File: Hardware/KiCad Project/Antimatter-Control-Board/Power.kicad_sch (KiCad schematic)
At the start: 5 parts, among them J1 3P JST XH, SW1 SW_SPST, U2 AP2210N-3.3TRG1

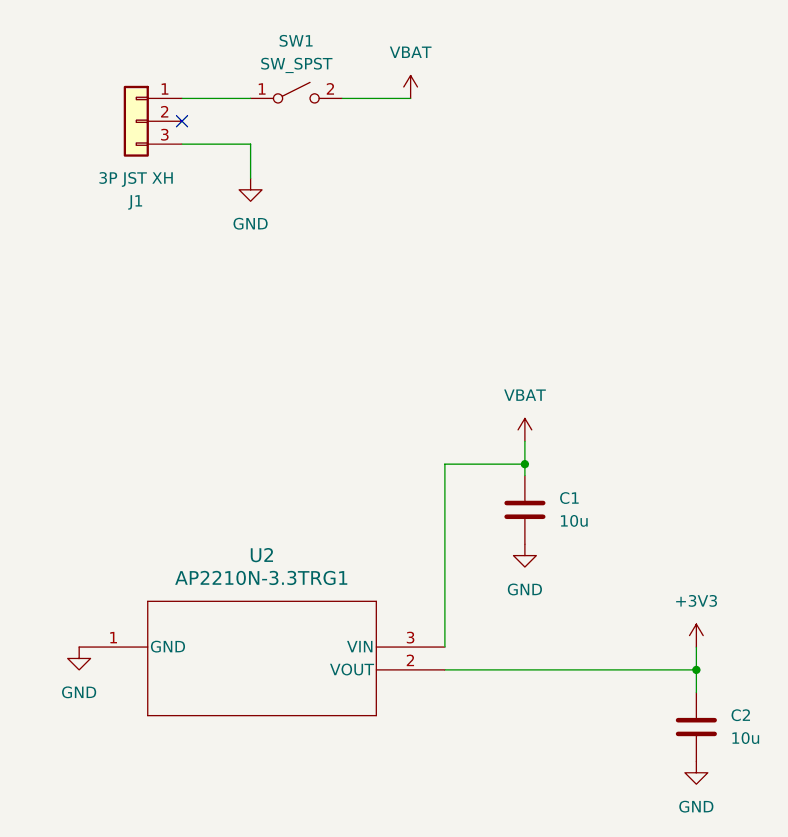
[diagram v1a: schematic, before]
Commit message: Add battery monitor divider and power led
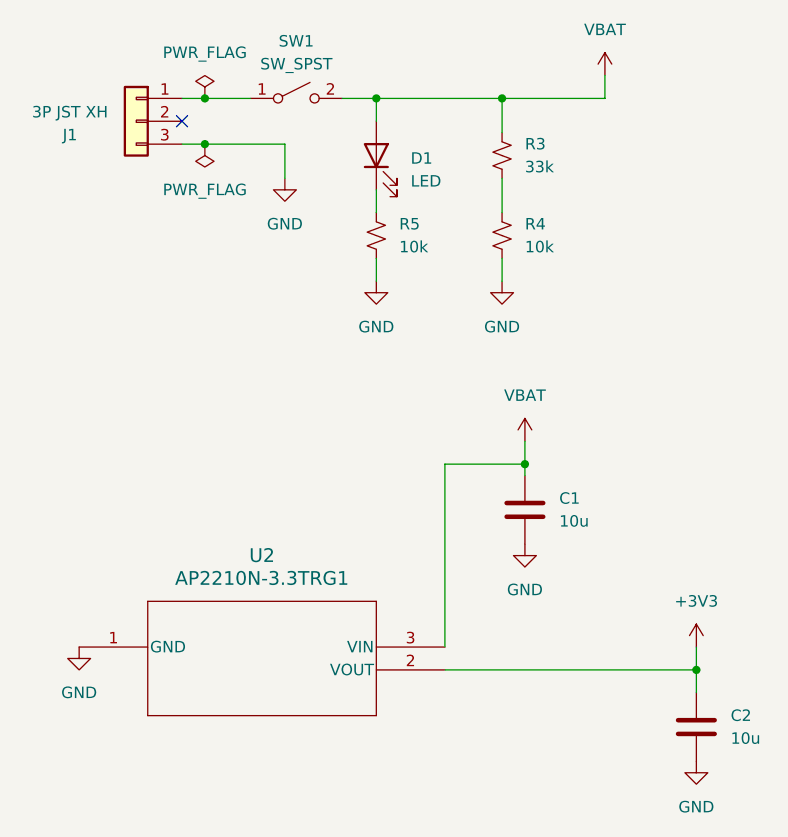
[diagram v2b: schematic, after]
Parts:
- added D1: LED, LED_THT:LED_D3.0mm, symbol Device:LED
- added R3: 33k, symbol Device:R_Small_US
- added R4, R5: 10k, symbol Device:R_Small_US
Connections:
- net GND: now also R4.2, R5.2
- net VBAT: now also D1.2 (A), R3.1
- new net: R3.2, R4.1
- new net: D1.1 (K), R5.1

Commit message: Connect up MCU
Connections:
- net BATT SENSE: now reaches R3.2, R4.1
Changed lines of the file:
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@@
+		)
+	)
+	(hierarchical_label "BATT SENSE"
+		(shape passive)
+		(at 128.27 58.42 0)
+		(effects
+			(font
+				(size 1.27 1.27)
+			)
+			(justify left)
 		)
 	)
